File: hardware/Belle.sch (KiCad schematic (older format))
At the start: 16 parts

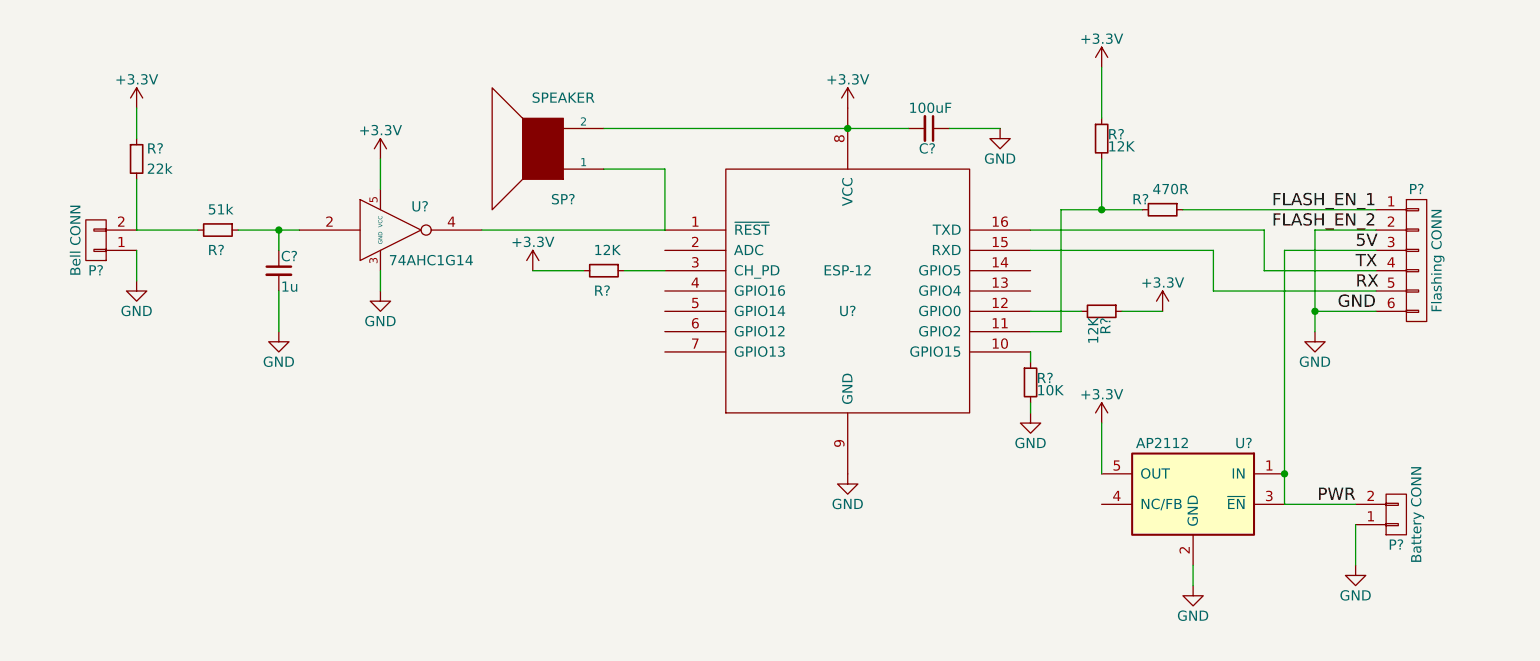
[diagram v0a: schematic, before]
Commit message: include ESP8266 library
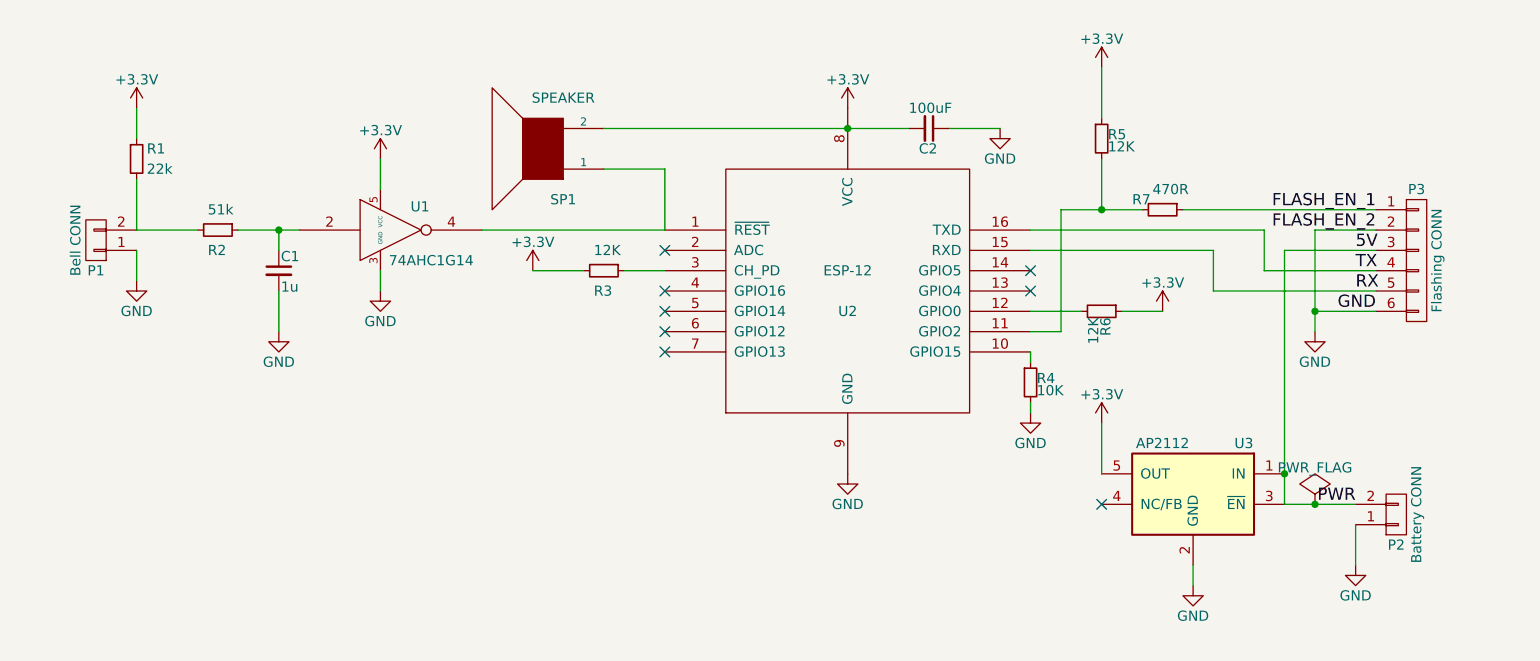
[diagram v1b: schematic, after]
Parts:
- C1, C2: renamed from C?; footprint (none) -> Capacitors_SMD:C_1206_HandSoldering
- P1: renamed from P?; footprint (none) -> Terminal_Blocks:TerminalBlock_Pheonix_MKDS1.5-2pol
- P2: renamed from P?; footprint (none) -> Pin_Headers:Pin_Header_Straight_1x02_Pitch2.54mm
- P3: renamed from P?; footprint (none) -> Pin_Headers:Pin_Header_Straight_1x06_Pitch2.54mm
- R1, R2, R3, R4, R5, R6, R7: renamed from R?; footprint (none) -> Resistors_SMD:R_1206_HandSoldering
- U1: renamed from U?; footprint (none) -> TO_SOT_Packages_SMD:SOT-23-5_HandSoldering
- U2: renamed from U?; footprint (none) -> ESP8266:ESP-12
- U3: renamed from U?; footprint SOT-23-5 -> TO_SOT_Packages_SMD:SOT-23-5_HandSoldering
- gave numbers to parts that had none: 1
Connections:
- no-connect marks 0 -> 8
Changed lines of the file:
@@
 LIBS:valves
 LIBS:Belle
-LIBS:ESP8266
+LIBS:Belle-cache
 EELAYER 25 0
 EELAYER END
@@
 $EndDescr
 $Comp
-L ESP-12 U?
+L ESP-12 U2
 U 1 1 58BBC183
 P 5900 3800
-F 0 "U?" H 5900 3700 50  0000 C CNN
+F 0 "U2" H 5900 3700 50  0000 C CNN
 F 1 "ESP-12" H 5900 3900 50  0000 C CNN
-F 2 "" H 5900 3800 50  0001 C CNN
+F 2 "ESP8266:ESP-12" H 5900 3800 50  0001 C CNN
 F 3 "" H 5900 3800 50  0001 C CNN
 	1    5900 3800
@@
 $EndComp
 $Comp
-L GND #PWR?
+L GND #PWR01
 U 1 1 58BBCCFC
 P 5900 4700
-F 0 "#PWR?" H 5900 4450 50  0001 C CNN
+F 0 "#PWR01" H 5900 4450 50  0001 C CNN
 F 1 "GND" H 5900 4550 50  0000 C CNN
 F 2 "" H 5900 4700 50  0000 C CNN
@@
 $EndComp
 $Comp
-L +3.3V #PWR?
+L +3.3V #PWR02
 U 1 1 58BBCD12
 P 5900 2900
-F 0 "#PWR?" H 5900 2750 50  0001 C CNN
+F 0 "#PWR02" H 5900 2750 50  0001 C CNN
 F 1 "+3.3V" H 5900 3040 50  0000 C CNN
 F 2 "" H 5900 2900 50  0000 C CNN
@@
 $EndComp
 $Comp
-L C_Small C?
+L C_Small C2
 U 1 1 58BBCD3B
 P 6300 3000
-F 0 "C?" V 6400 2950 50  0000 L CNN
+F 0 "C2" V 6400 2950 50  0000 L CNN
 F 1 "100uF" V 6200 2900 50  0000 L CNN
-F 2 "" H 6300 3000 50  0000 C CNN
+F 2 "Capacitors_SMD:C_1206_HandSoldering" H 6300 3000 50  0001 C CNN
 F 3 "" H 6300 3000 50  0000 C CNN
 	1    6300 3000
@@
 $EndComp
 $Comp
-L GND #PWR?
+L GND #PWR03
 U 1 1 58BBCDC5
 P 6650 3000
-F 0 "#PWR?" H 6650 2750 50  0001 C CNN
+F 0 "#PWR03" H 6650 2750 50  0001 C CNN
 F 1 "GND" H 6650 2850 50  0000 C CNN
 F 2 "" H 6650 3000 50  0000 C CNN
@@
 $EndComp
 $Comp
-L SPEAKER SP?
+L SPEAKER SP1
 U 1 1 58BBCE20
 P 4400 3100
-F 0 "SP?" H 4300 3350 50  0000 C CNN
+F 0 "SP1" H 4300 3350 50  0000 C CNN
 F 1 "SPEAKER" H 4300 2850 50  0000 C CNN
-F 2 "" H 4400 3100 50  0000 C CNN
+F 2 "" H 4400 3100 50  0001 C CNN
 F 3 "" H 4400 3100 50  0000 C CNN
 	1    4400 3100
@@
 $EndComp
 $Comp
-L 74AHC1G14 U?
+L 74AHC1G14 U1
 U 1 1 58BBCFA1
 P 3650 3500
-F 0 "U?" H 3795 3615 50  0000 C CNN
+F 0 "U1" H 3795 3615 50  0000 C CNN
 F 1 "74AHC1G14" H 3850 3350 50  0000 C CNN
-F 2 "" H 3745 3365 50  0000 C CNN
+F 2 "TO_SOT_Packages_SMD:SOT-23-5_HandSoldering" H 3745 3365 50  0001 C CNN
 F 3 "" H 3795 3615 50  0000 C CNN
 	1    3650 3500
@@
 $EndComp
 $Comp
-L GND #PWR?
+L GND #PWR04
 U 1 1 58BBD0DA
 P 3600 3800
-F 0 "#PWR?" H 3600 3550 50  0001 C CNN
+F 0 "#PWR04" H 3600 3550 50  0001 C CNN
 F 1 "GND" H 3600 3650 50  0000 C CNN
 F 2 "" H 3600 3800 50  0000 C CNN
@@
 $EndComp
 $Comp
-L +3.3V #PWR?
+L +3.3V #PWR05
 U 1 1 58BBD0F6
 P 3600 3150
-F 0 "#PWR?" H 3600 3000 50  0001 C CNN
+F 0 "#PWR05" H 3600 3000 50  0001 C CNN
 F 1 "+3.3V" H 3600 3290 50  0000 C CNN
 F 2 "" H 3600 3150 50  0000 C CNN
@@
 $EndComp
 $Comp
-L C_Small C?
+L C_Small C1
 U 1 1 58BBD184
 P 3100 3700
-F 0 "C?" H 3110 3770 50  0000 L CNN
+F 0 "C1" H 3110 3770 50  0000 L CNN
 F 1 "1u" H 3110 3620 50  0000 L CNN
-F 2 "" H 3100 3700 50  0000 C CNN
+F 2 "Capacitors_SMD:C_1206_HandSoldering" H 3100 3700 50  0001 C CNN
 F 3 "" H 3100 3700 50  0000 C CNN
 	1    3100 3700
@@
 $EndComp
 $Comp
-L GND #PWR?
+L GND #PWR06
 U 1 1 58BBD1A3
 P 3100 4000
-F 0 "#PWR?" H 3100 3750 50  0001 C CNN
+F 0 "#PWR06" H 3100 3750 50  0001 C CNN
 F 1 "GND" H 3100 3850 50  0000 C CNN
 F 2 "" H 3100 4000 50  0000 C CNN
@@
 $EndComp
 $Comp
-L R_Small R?
+L R_Small R2
 U 1 1 58BBD1C1
 P 2800 3500
-F 0 "R?" V 2900 3450 50  0000 L CNN
+F 0 "R2" V 2900 3450 50  0000 L CNN
 F 1 "51k" V 2700 3450 50  0000 L CNN
-F 2 "" H 2800 3500 50  0000 C CNN
+F 2 "Resistors_SMD:R_1206_HandSoldering" H 2800 3500 50  0001 C CNN
 F 3 "" H 2800 3500 50  0000 C CNN
 	1    2800 3500
@@
 $EndComp
 $Comp
-L R_Small R?
+L R_Small R1
 U 1 1 58BBD236
 P 2400 3150
-F 0 "R?" H 2450 3200 50  0000 L CNN
+F 0 "R1" H 2450 3200 50  0000 L CNN
 F 1 "22k" H 2450 3100 50  0000 L CNN
-F 2 "" H 2400 3150 50  0000 C CNN
+F 2 "Resistors_SMD:R_1206_HandSoldering" H 2400 3150 50  0001 C CNN
 F 3 "" H 2400 3150 50  0000 C CNN
 	1    2400 3150
@@
 $EndComp
 $Comp
-L +3.3V #PWR?
+L +3.3V #PWR07
 U 1 1 58BBD349
 P 2400 2900
-F 0 "#PWR?" H 2400 2750 50  0001 C CNN
+F 0 "#PWR07" H 2400 2750 50  0001 C CNN
 F 1 "+3.3V" H 2400 3040 50  0000 C CNN
 F 2 "" H 2400 2900 50  0000 C CNN
@@
 $EndComp
 $Comp
-L CONN_01X02 P?
+L CONN_01X02 P1
 U 1 1 58BBD41F
 P 2200 3550
-F 0 "P?" H 2200 3700 50  0000 C CNN
+F 0 "P1" H 2200 3700 50  0000 C CNN
 F 1 "Bell CONN" V 2300 3550 50  0000 C CNN
-F 2 "" H 2200 3550 50  0000 C CNN
+F 2 "Terminal_Blocks:TerminalBlock_Pheonix_MKDS1.5-2pol" H 2200 3550 50  0001 C CNN
 F 3 "" H 2200 3550 50  0000 C CNN
 	1    2200 3550
@@
 $EndComp
 $Comp
-L GND #PWR?
+L GND #PWR08
 U 1 1 58BBD44E
 P 2400 3750
-F 0 "#PWR?" H 2400 3500 50  0001 C CNN
+F 0 "#PWR08" H 2400 3500 50  0001 C CNN
 F 1 "GND" H 2400 3600 50  0000 C CNN
 F 2 "" H 2400 3750 50  0000 C CNN
@@
 $EndComp
 $Comp
-L +3.3V #PWR?
+L +3.3V #PWR09
 U 1 1 58BBD4B2
 P 4350 3700
-F 0 "#PWR?" H 4350 3550 50  0001 C CNN
+F 0 "#PWR09" H 4350 3550 50  0001 C CNN
 F 1 "+3.3V" H 4350 3840 50  0000 C CNN
 F 2 "" H 4350 3700 50  0000 C CNN
@@
 $EndComp
 $Comp
-L R_Small R?
+L R_Small R3
 U 1 1 58BBD531
 P 4700 3700
-F 0 "R?" V 4800 3650 50  0000 L CNN
+F 0 "R3" V 4800 3650 50  0000 L CNN
 F 1 "12K" V 4600 3650 50  0000 L CNN
-F 2 "" H 4700 3700 50  0000 C CNN
+F 2 "Resistors_SMD:R_1206_HandSoldering" H 4700 3700 50  0001 C CNN
 F 3 "" H 4700 3700 50  0000 C CNN
 	1    4700 3700
@@
 $EndComp
 $Comp
-L +3.3V #PWR?
+L +3.3V #PWR010
 U 1 1 58BBD5B6
 P 7450 3900
-F 0 "#PWR?" H 7450 3750 50  0001 C CNN
+F 0 "#PWR010" H 7450 3750 50  0001 C CNN
 F 1 "+3.3V" H 7450 4040 50  0000 C CNN
 F 2 "" H 7450 3900 50  0000 C CNN
@@
 $EndComp
 $Comp
-L R_Small R?
+L R_Small R6
 U 1 1 58BBD5DC
 P 7150 3900
-F 0 "R?" H 7180 3920 50  0000 L CNN
+F 0 "R6" H 7180 3920 50  0000 L CNN
 F 1 "12K" H 7180 3860 50  0000 L CNN
-F 2 "" H 7150 3900 50  0000 C CNN
+F 2 "Resistors_SMD:R_1206_HandSoldering" H 7150 3900 50  0001 C CNN
 F 3 "" H 7150 3900 50  0000 C CNN
 	1    7150 3900
@@
 $EndComp
 $Comp
-L GND #PWR?
+L GND #PWR011
 U 1 1 58BBD6CB
 P 6800 4400
-F 0 "#PWR?" H 6800 4150 50  0001 C CNN
+F 0 "#PWR011" H 6800 4150 50  0001 C CNN
 F 1 "GND" H 6800 4250 50  0000 C CNN
 F 2 "" H 6800 4400 50  0000 C CNN
@@
 $EndComp
 $Comp
-L R_Small R?
+L R_Small R4
 U 1 1 58BBD6F3
 P 6800 4250
-F 0 "R?" H 6830 4270 50  0000 L CNN
+F 0 "R4" H 6830 4270 50  0000 L CNN
 F 1 "10K" H 6830 4210 50  0000 L CNN
-F 2 "" H 6800 4250 50  0000 C CNN
+F 2 "Resistors_SMD:R_1206_HandSoldering" H 6800 4250 50  0001 C CNN
 F 3 "" H 6800 4250 50  0000 C CNN
 	1    6800 4250
@@
 $EndComp
 $Comp
-L TPS769XX U?
+L TPS769XX U3
 U 1 1 58BBD7D2
 P 7600 4850
-F 0 "U?" H 7350 5150 50  0000 C CNN
+F 0 "U3" H 7350 5150 50  0000 C CNN
 F 1 "AP2112" H 7750 5150 50  0000 C CNN
-F 2 "SOT-23-5" H 7600 4950 50  0001 C CIN
+F 2 "TO_SOT_Packages_SMD:SOT-23-5_HandSoldering" H 7600 4950 50  0001 C CIN
 F 3 "" H 7600 4850 50  0000 C CNN
 	1    7600 4850
@@
 $EndComp
 $Comp
-L +3.3V #PWR?
+L +3.3V #PWR012
 U 1 1 58BBDA6C
 P 7150 4450
-F 0 "#PWR?" H 7150 4300 50  0001 C CNN
+F 0 "#PWR012" H 7150 4300 50  0001 C CNN
 F 1 "+3.3V" H 7150 4590 50  0000 C CNN
 F 2 "" H 7150 4450 50  0000 C CNN
@@
 $EndComp
 $Comp
-L CONN_01X02 P?
+L CONN_01X02 P2
 U 1 1 58BBDA98
 P 8600 4900
-F 0 "P?" H 8600 5050 50  0000 C CNN
+F 0 "P2" H 8600 5050 50  0000 C CNN
 F 1 "Battery CONN" V 8700 4900 50  0000 C CNN
-F 2 "" H 8600 4900 50  0000 C CNN
+F 2 "Pin_Headers:Pin_Header_Straight_1x02_Pitch2.54mm" H 8600 4900 50  0001 C CNN
 F 3 "" H 8600 4900 50  0000 C CNN
 	1    8600 4900
@@
 $EndComp
 $Comp
-L GND #PWR?
+L GND #PWR013
 U 1 1 58BBDB81
 P 7600 5250
-F 0 "#PWR?" H 7600 5000 50  0001 C CNN
+F 0 "#PWR013" H 7600 5000 50  0001 C CNN
 F 1 "GND" H 7600 5100 50  0000 C CNN
 F 2 "" H 7600 5250 50  0000 C CNN
@@
 $EndComp
 $Comp
-L GND #PWR?
+L GND #PWR014
 U 1 1 58BBDD34
 P 8400 5150
-F 0 "#PWR?" H 8400 4900 50  0001 C CNN
+F 0 "#PWR014" H 8400 4900 50  0001 C CNN
 F 1 "GND" H 8400 5000 50  0000 C CNN
 F 2 "" H 8400 5150 50  0000 C CNN
@@
 $EndComp
 $Comp
-L CONN_01X06 P?
+L CONN_01X06 P3
 U 1 1 58BBDEAA
 P 8700 3650
-F 0 "P?" H 8700 4000 50  0000 C CNN
+F 0 "P3" H 8700 4000 50  0000 C CNN
 F 1 "Flashing CONN" V 8800 3650 50  0000 C CNN
-F 2 "" H 8700 3650 50  0000 C CNN
+F 2 "Pin_Headers:Pin_Header_Straight_1x06_Pitch2.54mm" H 8700 3650 50  0001 C CNN
 F 3 "" H 8700 3650 50  0000 C CNN
 	1    8700 3650
@@
 $EndComp
 $Comp
-L GND #PWR?
+L GND #PWR015
 U 1 1 58BBDF88
 P 8200 4000
-F 0 "#PWR?" H 8200 3750 50  0001 C CNN
+F 0 "#PWR015" H 8200 3750 50  0001 C CNN
 F 1 "GND" H 8200 3850 50  0000 C CNN
 F 2 "" H 8200 4000 50  0000 C CNN
@@
 	6950 3400 7350 3400
 $Comp
-L R_Small R?
+L R_Small R7
 U 1 1 58BBEBD8
 P 7450 3400
-F 0 "R?" V 7400 3250 50  0000 L CNN
+F 0 "R7" V 7400 3250 50  0000 L CNN
 F 1 "470R" V 7350 3350 50  0000 L CNN
-F 2 "" H 7450 3400 50  0000 C CNN
+F 2 "Resistors_SMD:R_1206_HandSoldering" H 7450 3400 50  0001 C CNN
 F 3 "" H 7450 3400 50  0000 C CNN
 	1    7450 3400
@@
 	7550 3400 8500 3400
 $Comp
-L R_Small R?
+L R_Small R5
 U 1 1 58BBEC6E
 P 7150 3050
-F 0 "R?" H 7180 3070 50  0000 L CNN
+F 0 "R5" H 7180 3070 50  0000 L CNN
 F 1 "12K" H 7180 3010 50  0000 L CNN
-F 2 "" H 7150 3050 50  0000 C CNN
+F 2 "Resistors_SMD:R_1206_HandSoldering" H 7150 3050 50  0001 C CNN
 F 3 "" H 7150 3050 50  0000 C CNN
 	1    7150 3050
@@
 $EndComp
 $Comp
-L +3.3V #PWR?
+L +3.3V #PWR016
 U 1 1 58BBED05
 P 7150 2700
-F 0 "#PWR?" H 7150 2550 50  0001 C CNN
+F 0 "#PWR016" H 7150 2550 50  0001 C CNN
 F 1 "+3.3V" H 7150 2840 50  0000 C CNN
 F 2 "" H 7150 2700 50  0000 C CNN
@@
 Text Label 8400 4850 2    60   ~ 0
 PWR
+NoConn ~ 5000 4100
+NoConn ~ 5000 4000
+NoConn ~ 5000 3900
+NoConn ~ 5000 3800
+NoConn ~ 5000 3600
+NoConn ~ 7150 4850
+NoConn ~ 6800 3700
+NoConn ~ 6800 3800
+$Comp
+L PWR_FLAG #FLG017
+U 1 1 58BBEBAB
+P 8200 4850
+F 0 "#FLG017" H 8200 4945 50  0001 C CNN
+F 1 "PWR_FLAG" H 8200 5030 50  0000 C CNN
+F 2 "" H 8200 4850 50  0000 C CNN
+F 3 "" H 8200 4850 50  0000 C CNN
+	1    8200 4850
+	1    0    0    -1
+$EndComp
+Connection ~ 8200 4850
 $EndSCHEMATC

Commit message: regenerated gerbers
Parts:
- C2: value 100uF -> 10uF
- SP1: footprint (none) -> Belle:prosignal_buzzer
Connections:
- net +3V3: now also C2.2, SP1.2
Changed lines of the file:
@@
 LIBS:valves
 LIBS:Belle
+LIBS:ESP8266
 LIBS:Belle-cache
 EELAYER 25 0
@@
 L +3.3V #PWR02
 U 1 1 58BBCD12
-P 5900 2900
-F 0 "#PWR02" H 5900 2750 50  0001 C CNN
-F 1 "+3.3V" H 5900 3040 50  0000 C CNN
-F 2 "" H 5900 2900 50  0000 C CNN
-F 3 "" H 5900 2900 50  0000 C CNN
-	1    5900 2900
+P 5900 2800
+F 0 "#PWR02" H 5900 2650 50  0001 C CNN
+F 1 "+3.3V" H 5900 2940 50  0000 C CNN
+F 2 "" H 5900 2800 50  0000 C CNN
+F 3 "" H 5900 2800 50  0000 C CNN
+	1    5900 2800
 	1    0    0    -1
 $EndComp
@@
 P 6300 3000
 F 0 "C2" V 6400 2950 50  0000 L CNN
-F 1 "100uF" V 6200 2900 50  0000 L CNN
+F 1 "10uF" V 6200 2900 50  0000 L CNN
 F 2 "Capacitors_SMD:C_1206_HandSoldering" H 6300 3000 50  0001 C CNN
 F 3 "" H 6300 3000 50  0000 C CNN
@@
 F 0 "SP1" H 4300 3350 50  0000 C CNN
 F 1 "SPEAKER" H 4300 2850 50  0000 C CNN
-F 2 "" H 4400 3100 50  0001 C CNN
+F 2 "Belle:prosignal_buzzer" H 4400 3100 50  0001 C CNN
 F 3 "" H 4400 3100 50  0000 C CNN
 	1    4400 3100
@@
 RX
 Wire Wire Line
-	4700 3000 6200 3000
-Wire Wire Line
 	6400 3000 6650 3000
 Wire Wire Line
@@
 	7150 3150 7150 3400
 Connection ~ 7150 3400
-Connection ~ 5900 3000
 Text Label 8400 3600 0    60   ~ 0
 5V
@@
 $EndComp
 Connection ~ 8200 4850
+Wire Wire Line
+	6200 2900 6200 3000
+Wire Wire Line
+	4700 2900 6200 2900
+Wire Wire Line
+	5900 2900 5900 2800
+Wire Wire Line
+	4700 2900 4700 3000
+Connection ~ 5900 2900
 $EndSCHEMATC

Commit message: edit layout. close #1
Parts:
- added C3, C4: 1u, symbol C_Small
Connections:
- net +3V3: now also C3.1
- net 5V: now also C4.2
- net GND: now also C3.2, C4.1
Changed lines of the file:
@@
 $EndComp
 $Comp
-L GND #PWR01
+L GND #PWR8
 U 1 1 58BBCCFC
 P 5900 4700
-F 0 "#PWR01" H 5900 4450 50  0001 C CNN
+F 0 "#PWR8" H 5900 4450 50  0001 C CNN
 F 1 "GND" H 5900 4550 50  0000 C CNN
 F 2 "" H 5900 4700 50  0000 C CNN
@@
 $EndComp
 $Comp
-L +3.3V #PWR02
+L +3.3V #PWR7
 U 1 1 58BBCD12
 P 5900 2800
-F 0 "#PWR02" H 5900 2650 50  0001 C CNN
+F 0 "#PWR7" H 5900 2650 50  0001 C CNN
 F 1 "+3.3V" H 5900 2940 50  0000 C CNN
 F 2 "" H 5900 2800 50  0000 C CNN
@@
 $EndComp
 $Comp
-L GND #PWR03
+L GND #PWR9
 U 1 1 58BBCDC5
 P 6650 3000
-F 0 "#PWR03" H 6650 2750 50  0001 C CNN
+F 0 "#PWR9" H 6650 2750 50  0001 C CNN
 F 1 "GND" H 6650 2850 50  0000 C CNN
 F 2 "" H 6650 3000 50  0000 C CNN
@@
 $EndComp
 $Comp
-L GND #PWR04
+L GND #PWR5
 U 1 1 58BBD0DA
 P 3600 3800
-F 0 "#PWR04" H 3600 3550 50  0001 C CNN
+F 0 "#PWR5" H 3600 3550 50  0001 C CNN
 F 1 "GND" H 3600 3650 50  0000 C CNN
 F 2 "" H 3600 3800 50  0000 C CNN
@@
 $EndComp
 $Comp
-L +3.3V #PWR05
+L +3.3V #PWR4
 U 1 1 58BBD0F6
 P 3600 3150
-F 0 "#PWR05" H 3600 3000 50  0001 C CNN
+F 0 "#PWR4" H 3600 3000 50  0001 C CNN
 F 1 "+3.3V" H 3600 3290 50  0000 C CNN
 F 2 "" H 3600 3150 50  0000 C CNN
@@
 $EndComp
 $Comp
-L GND #PWR06
+L GND #PWR3
 U 1 1 58BBD1A3
 P 3100 4000
-F 0 "#PWR06" H 3100 3750 50  0001 C CNN
+F 0 "#PWR3" H 3100 3750 50  0001 C CNN
 F 1 "GND" H 3100 3850 50  0000 C CNN
 F 2 "" H 3100 4000 50  0000 C CNN
@@
 $EndComp
 $Comp
-L +3.3V #PWR07
+L +3.3V #PWR1
 U 1 1 58BBD349
 P 2400 2900
-F 0 "#PWR07" H 2400 2750 50  0001 C CNN
+F 0 "#PWR1" H 2400 2750 50  0001 C CNN
 F 1 "+3.3V" H 2400 3040 50  0000 C CNN
 F 2 "" H 2400 2900 50  0000 C CNN
@@
 $EndComp
 $Comp
-L GND #PWR08
+L GND #PWR2
 U 1 1 58BBD44E
 P 2400 3750
-F 0 "#PWR08" H 2400 3500 50  0001 C CNN
+F 0 "#PWR2" H 2400 3500 50  0001 C CNN
 F 1 "GND" H 2400 3600 50  0000 C CNN
 F 2 "" H 2400 3750 50  0000 C CNN
@@
 $EndComp
 $Comp
-L +3.3V #PWR09
+L +3.3V #PWR6
 U 1 1 58BBD4B2
 P 4350 3700
-F 0 "#PWR09" H 4350 3550 50  0001 C CNN
+F 0 "#PWR6" H 4350 3550 50  0001 C CNN
 F 1 "+3.3V" H 4350 3840 50  0000 C CNN
 F 2 "" H 4350 3700 50  0000 C CNN
@@
 $EndComp
 $Comp
-L +3.3V #PWR010
+L +3.3V #PWR14
 U 1 1 58BBD5B6
 P 7450 3900
-F 0 "#PWR010" H 7450 3750 50  0001 C CNN
+F 0 "#PWR14" H 7450 3750 50  0001 C CNN
 F 1 "+3.3V" H 7450 4040 50  0000 C CNN
 F 2 "" H 7450 3900 50  0000 C CNN
@@
 $EndComp
 $Comp
-L GND #PWR011
+L GND #PWR10
 U 1 1 58BBD6CB
 P 6800 4400
-F 0 "#PWR011" H 6800 4150 50  0001 C CNN
+F 0 "#PWR10" H 6800 4150 50  0001 C CNN
 F 1 "GND" H 6800 4250 50  0000 C CNN
 F 2 "" H 6800 4400 50  0000 C CNN
@@
 $EndComp
 $Comp
-L +3.3V #PWR012
+L +3.3V #PWR13
 U 1 1 58BBDA6C
 P 7150 4450
-F 0 "#PWR012" H 7150 4300 50  0001 C CNN
+F 0 "#PWR13" H 7150 4300 50  0001 C CNN
 F 1 "+3.3V" H 7150 4590 50  0000 C CNN
 F 2 "" H 7150 4450 50  0000 C CNN
@@
 $EndComp
 $Comp
-L GND #PWR013
+L GND #PWR15
 U 1 1 58BBDB81
 P 7600 5250
-F 0 "#PWR013" H 7600 5000 50  0001 C CNN
+F 0 "#PWR15" H 7600 5000 50  0001 C CNN
 F 1 "GND" H 7600 5100 50  0000 C CNN
 F 2 "" H 7600 5250 50  0000 C CNN
@@
 $EndComp
 $Comp
-L GND #PWR014
+L GND #PWR17
 U 1 1 58BBDD34
 P 8400 5150
-F 0 "#PWR014" H 8400 4900 50  0001 C CNN
+F 0 "#PWR17" H 8400 4900 50  0001 C CNN
 F 1 "GND" H 8400 5000 50  0000 C CNN
 F 2 "" H 8400 5150 50  0000 C CNN
@@
 $EndComp
 $Comp
-L GND #PWR015
+L GND #PWR16
 U 1 1 58BBDF88
 P 8200 4000
-F 0 "#PWR015" H 8200 3750 50  0001 C CNN
+F 0 "#PWR16" H 8200 3750 50  0001 C CNN
 F 1 "GND" H 8200 3850 50  0000 C CNN
 F 2 "" H 8200 4000 50  0000 C CNN
@@
 $EndComp
 $Comp
-L +3.3V #PWR016
+L +3.3V #PWR12
 U 1 1 58BBED05
 P 7150 2700
-F 0 "#PWR016" H 7150 2550 50  0001 C CNN
+F 0 "#PWR12" H 7150 2550 50  0001 C CNN
 F 1 "+3.3V" H 7150 2840 50  0000 C CNN
 F 2 "" H 7150 2700 50  0000 C CNN
@@
 NoConn ~ 6800 3800
 $Comp
-L PWR_FLAG #FLG017
+L PWR_FLAG #FLG1
 U 1 1 58BBEBAB
 P 8200 4850
-F 0 "#FLG017" H 8200 4945 50  0001 C CNN
+F 0 "#FLG1" H 8200 4945 50  0001 C CNN
 F 1 "PWR_FLAG" H 8200 5030 50  0000 C CNN
 F 2 "" H 8200 4850 50  0000 C CNN
@@
 	4700 2900 4700 3000
 Connection ~ 5900 2900
+$Comp
+L C_Small C4
+U 1 1 58CE4E44
+P 8300 4300
+F 0 "C4" H 8310 4370 50  0000 L CNN
+F 1 "1u" H 8310 4220 50  0000 L CNN
+F 2 "" H 8300 4300 50  0000 C CNN
+F 3 "" H 8300 4300 50  0000 C CNN
+	1    8300 4300
+	0    1    1    0
+$EndComp
+Wire Wire Line
+	8200 4300 8050 4300
+Connection ~ 8050 4300
+$Comp
+L GND #PWR18
+U 1 1 58CE4ED3
+P 8500 4300
+F 0 "#PWR18" H 8500 4050 50  0001 C CNN
+F 1 "GND" H 8500 4150 50  0000 C CNN
+F 2 "" H 8500 4300 50  0000 C CNN
+F 3 "" H 8500 4300 50  0000 C CNN
+	1    8500 4300
+	1    0    0    -1
+$EndComp
+Wire Wire Line
+	8400 4300 8500 4300
+$Comp
+L C_Small C3
+U 1 1 58CE500B
+P 6800 4800
+F 0 "C3" H 6810 4870 50  0000 L CNN
+F 1 "1u" H 6810 4720 50  0000 L CNN
+F 2 "" H 6800 4800 50  0000 C CNN
+F 3 "" H 6800 4800 50  0000 C CNN
+	1    6800 4800
+	1    0    0    -1
+$EndComp
+$Comp
+L GND #PWR11
+U 1 1 58CE504A
+P 6800 5000
+F 0 "#PWR11" H 6800 4750 50  0001 C CNN
+F 1 "GND" H 6800 4850 50  0000 C CNN
+F 2 "" H 6800 5000 50  0000 C CNN
+F 3 "" H 6800 5000 50  0000 C CNN
+	1    6800 5000
+	1    0    0    -1
+$EndComp
+Wire Wire Line
+	7150 4700 6800 4700
+Wire Wire Line
+	6800 4900 6800 5000
 $EndSCHEMATC
